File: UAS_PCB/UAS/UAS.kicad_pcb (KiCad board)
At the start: 2 copper layers, 50.8 x 47.6 mm, 17 parts, among them J1 SM02B-PASS-TBT, J2 SM02B-PASS-TBT, J3 SM02B-PASS-TBT, J4 SM02B-PASS-TBT, U1 JST-7-Pin, U10 UAS-rescue_7.5V-2.4A-Converte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, U11 JST-3-Pin, U12 Signal-Pad, U13 Signal-Pad, U2 5A-5V-Converter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

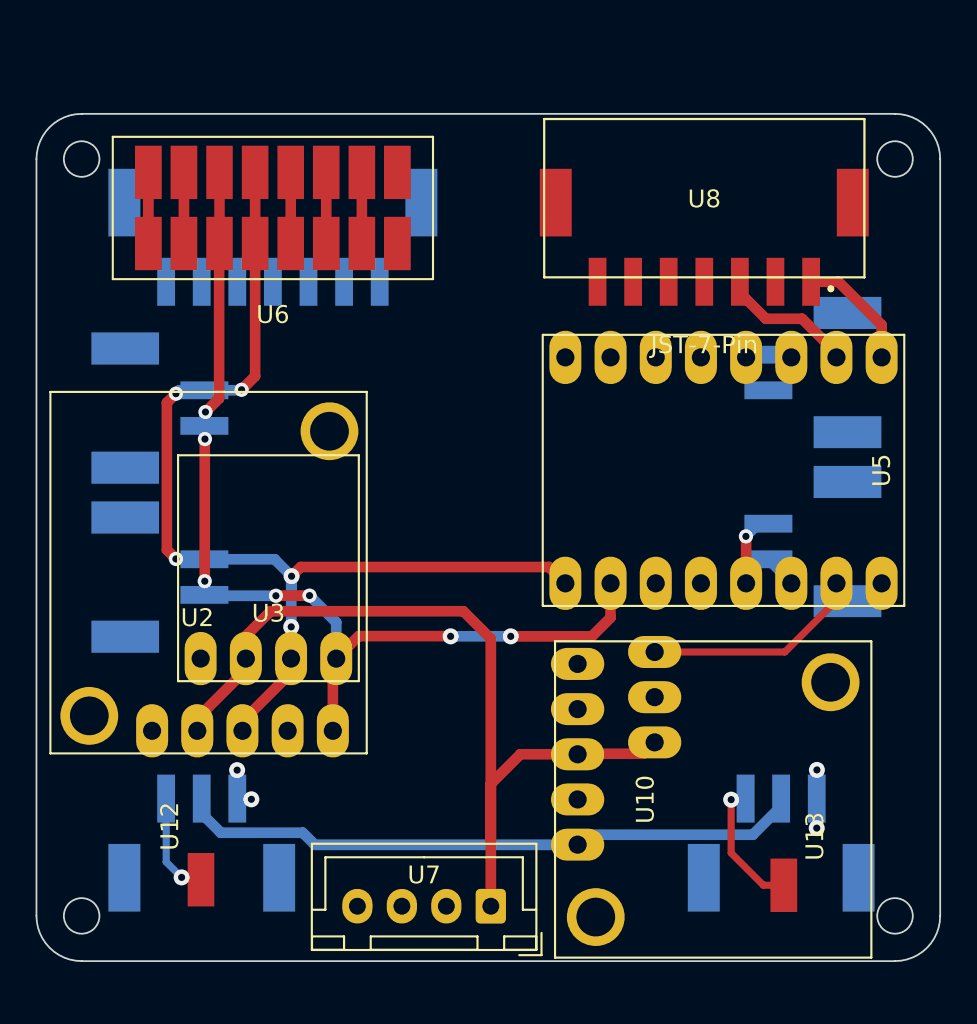
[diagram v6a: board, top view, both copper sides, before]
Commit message: slight rearranging and pin changes, PCS connector on top still needs to be reorganized for a straight shot
also, for gods sake we gotta change the symbols for connectors on the diagram
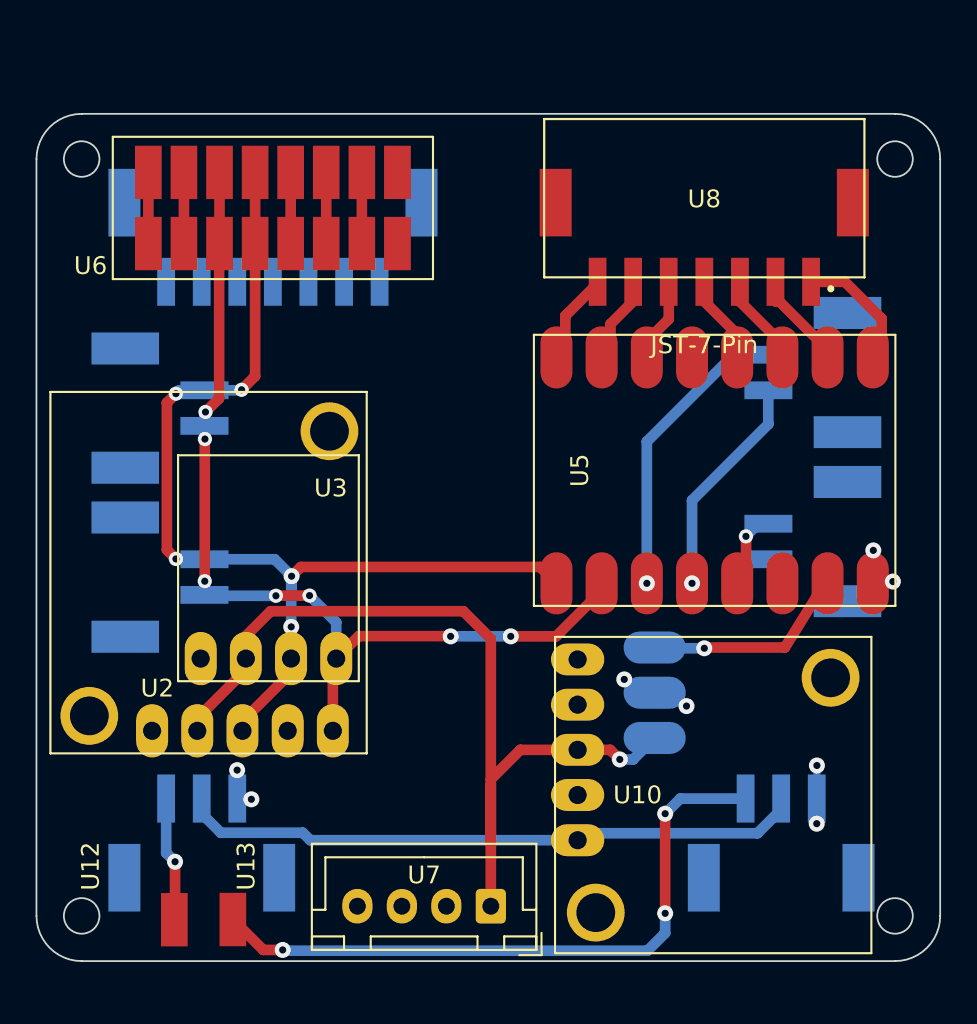
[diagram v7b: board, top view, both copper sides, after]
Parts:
- U4: footprint UAS:Pololu_12V_Step_Up_Voltage_Regulator -> UAS:Pololu_12V_Step_Up_Voltage_Regulator_SMT
- U5: footprint UAS:Pololu_TB6612_Dual_Motor_Driver_Carrier -> UAS:Pololu_TB6612_Dual_Motor_Driver_Carrier_SMT
- moved U13 31.0 mm to (128.5, 118.8)
- moved U12 2.70 mm to (125.2, 118.8)
- moved U5 0.50 mm to (150.5, 93.5)
- moved U10 0.25 mm to (155.5, 111.8)
- moved U4 0.25 mm to (154.8, 106.0)
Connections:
- J3 pad 2: Net-(J3-Pad2) -> GND
- J4 pad 2: Net-(J3-Pad2) -> GND
- U2 pad 3: Net-(J3-Pad2) -> GND
- U3 pad 3: Net-(J3-Pad2) -> GND
- U5 pad 1: Net-(J3-Pad2) -> GND
- U5 pad 3: Net-(J1-Pad2) -> Net-(J1-Pad1)
- U5 pad 4: Net-(J1-Pad1) -> Net-(J1-Pad2)
- U6 pad 10: Net-(J3-Pad2) -> GND
- U6 pad 9: Net-(J3-Pad2) -> GND
- U8 pad 2: Net-(U5-Pad9) -> Net-(U5-Pad15)
- U8 pad 3: Net-(U5-Pad15) -> Net-(U5-Pad14)
- U8 pad 4: Net-(U5-Pad11) -> Net-(U5-Pad13)
- U8 pad 5: Net-(U5-Pad10) -> Net-(U5-Pad11)
- U8 pad 6: Net-(U5-Pad13) -> Net-(U5-Pad10)
- U8 pad 7: Net-(U5-Pad14) -> Net-(U5-Pad9)
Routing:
- net Net-(J3-Pad2): track 59.7 -> 0.00 mm, vias 5 -> 0
- net GND: track 5.71 -> 64.9 mm, vias 4 -> 13
- net Net-(U13-Pad1): track 7.55 -> 37.1 mm, vias 1 -> 3
- net Net-(J1-Pad1): track 0.00 -> 16.8 mm, vias 0 -> 1
- net Net-(J1-Pad2): track 0.00 -> 12.6 mm, vias 0 -> 1
- net Net-(U5-Pad14): track 0.00 -> 6.07 mm
- net Net-(U5-Pad13): track 0.00 -> 5.22 mm
- net Net-(U5-Pad9): track 0.00 -> 5.00 mm
- net Net-(U5-Pad10): track 0.00 -> 4.78 mm
- net Net-(U5-Pad11): track 0.00 -> 4.55 mm
- net Net-(U10-Pad5): track 38.6 -> 40.3 mm
- net Net-(U5-Pad15): track 7.69 -> 6.07 mm
- net Net-(U11-Pad3): track 5.93 -> 7.03 mm
- net Net-(U10-Pad3): track 49.9 -> 50.4 mm, vias 0 -> 1
- net Net-(U4-Pad3): vias 0 -> 1

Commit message: fixed connector, 12v trace needs to be bigger for sure , probably close to 1.5mm
symbols are still messy FeelsBadMan
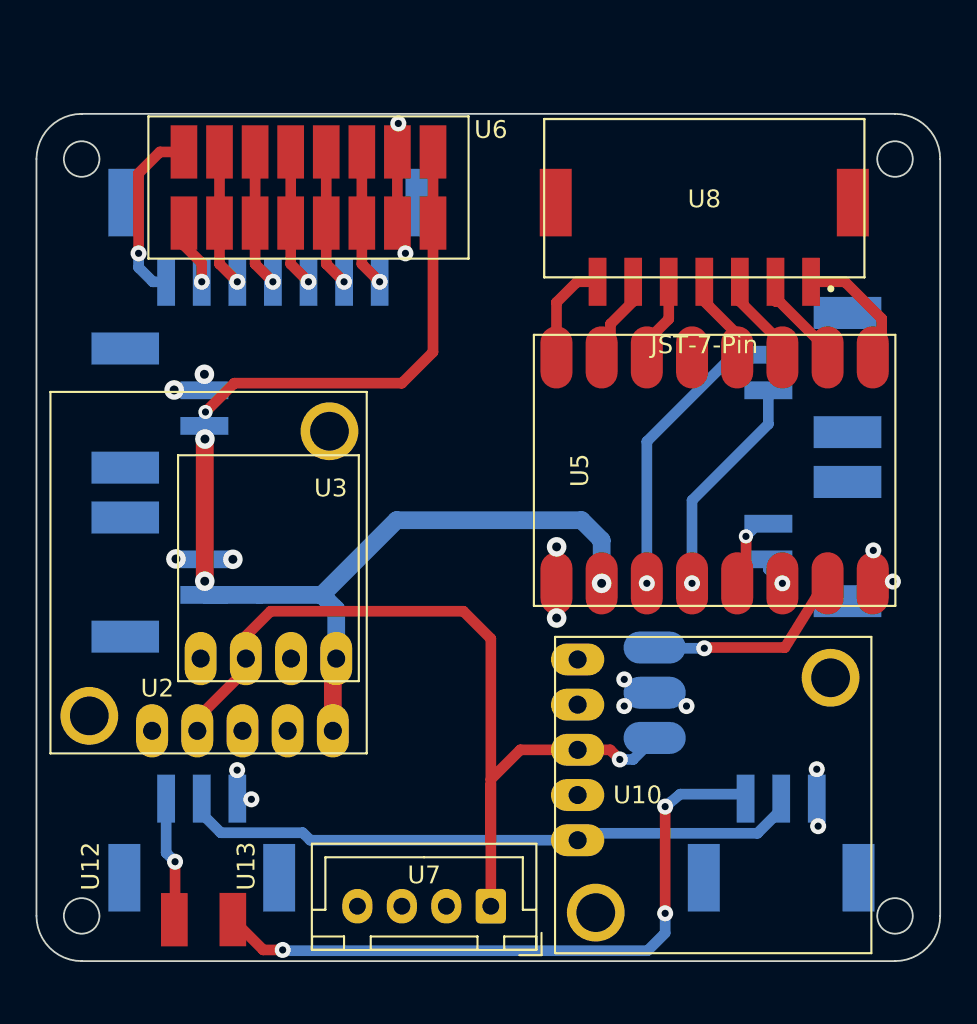
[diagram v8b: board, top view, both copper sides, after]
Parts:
- U6: value 16_Pad_2x8_Set -> 16_Pad_2x8_Set-UAS-cache
- moved U6 3.48 mm to (132.8, 79.6), turned to 0 degrees
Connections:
- net Net-(U10-Pad3) renamed +12V
- net Net-(U10-Pad5) renamed +7.5V
- J3 pad 1: Net-(J3-Pad1) -> +5V
- J4 pad 1: Net-(J3-Pad1) -> +5V
- U2 pad 5: Net-(J3-Pad1) -> +5V
- U3 pad 4: Net-(J3-Pad1) -> +5V
- U5 pad 2: Net-(J3-Pad1) -> +5V
- U6 pad 10: GND -> Net-(U1-Pad6)
- U6 pad 11: Net-(J3-Pad1) -> Net-(U1-Pad7)
- U6 pad 12: Net-(J3-Pad1) -> Net-(U1-Pad7)
- U6 pad 13: Net-(U1-Pad6) -> GND
- U6 pad 14: Net-(U1-Pad6) -> GND
- U6 pad 15: Net-(U1-Pad7) -> +5V
- U6 pad 16: Net-(U1-Pad7) -> +5V
- U6 pad 9: GND -> Net-(U1-Pad6)
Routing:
- net +5V: track 0.00 -> 72.7 mm, vias 0 -> 4
- net Net-(J3-Pad1): track 56.8 -> 0.00 mm, vias 7 -> 0
- net GND: track 64.9 -> 12.6 mm, vias 13 -> 17
- net Net-(U1-Pad1): track 0.00 -> 10.2 mm, vias 0 -> 1
- net Net-(U1-Pad7): track 4.00 -> 7.71 mm, vias 0 -> 1
- net Net-(U1-Pad6): track 4.00 -> 7.71 mm, vias 0 -> 1
- net Net-(U1-Pad5): track 4.00 -> 7.71 mm, vias 0 -> 1
- net Net-(U1-Pad4): track 4.00 -> 7.71 mm, vias 0 -> 1
- net Net-(U1-Pad3): track 4.00 -> 7.71 mm, vias 0 -> 1
- net Net-(U1-Pad2): track 0.00 -> 3.71 mm, vias 0 -> 1
- net Net-(U5-Pad9): track 5.00 -> 5.98 mm
- net Net-(J2-Pad2): track 1.88 -> 1.68 mm, vias 0 -> 1
